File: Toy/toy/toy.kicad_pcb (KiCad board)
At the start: 2 copper layers, 190 x 120 mm, 25 parts, among them J1 Conn_01x07_Pin, J2 Conn_01x03_Pin, J3 Conn_01x03_Pin, J4 Conn_01x03_Pin

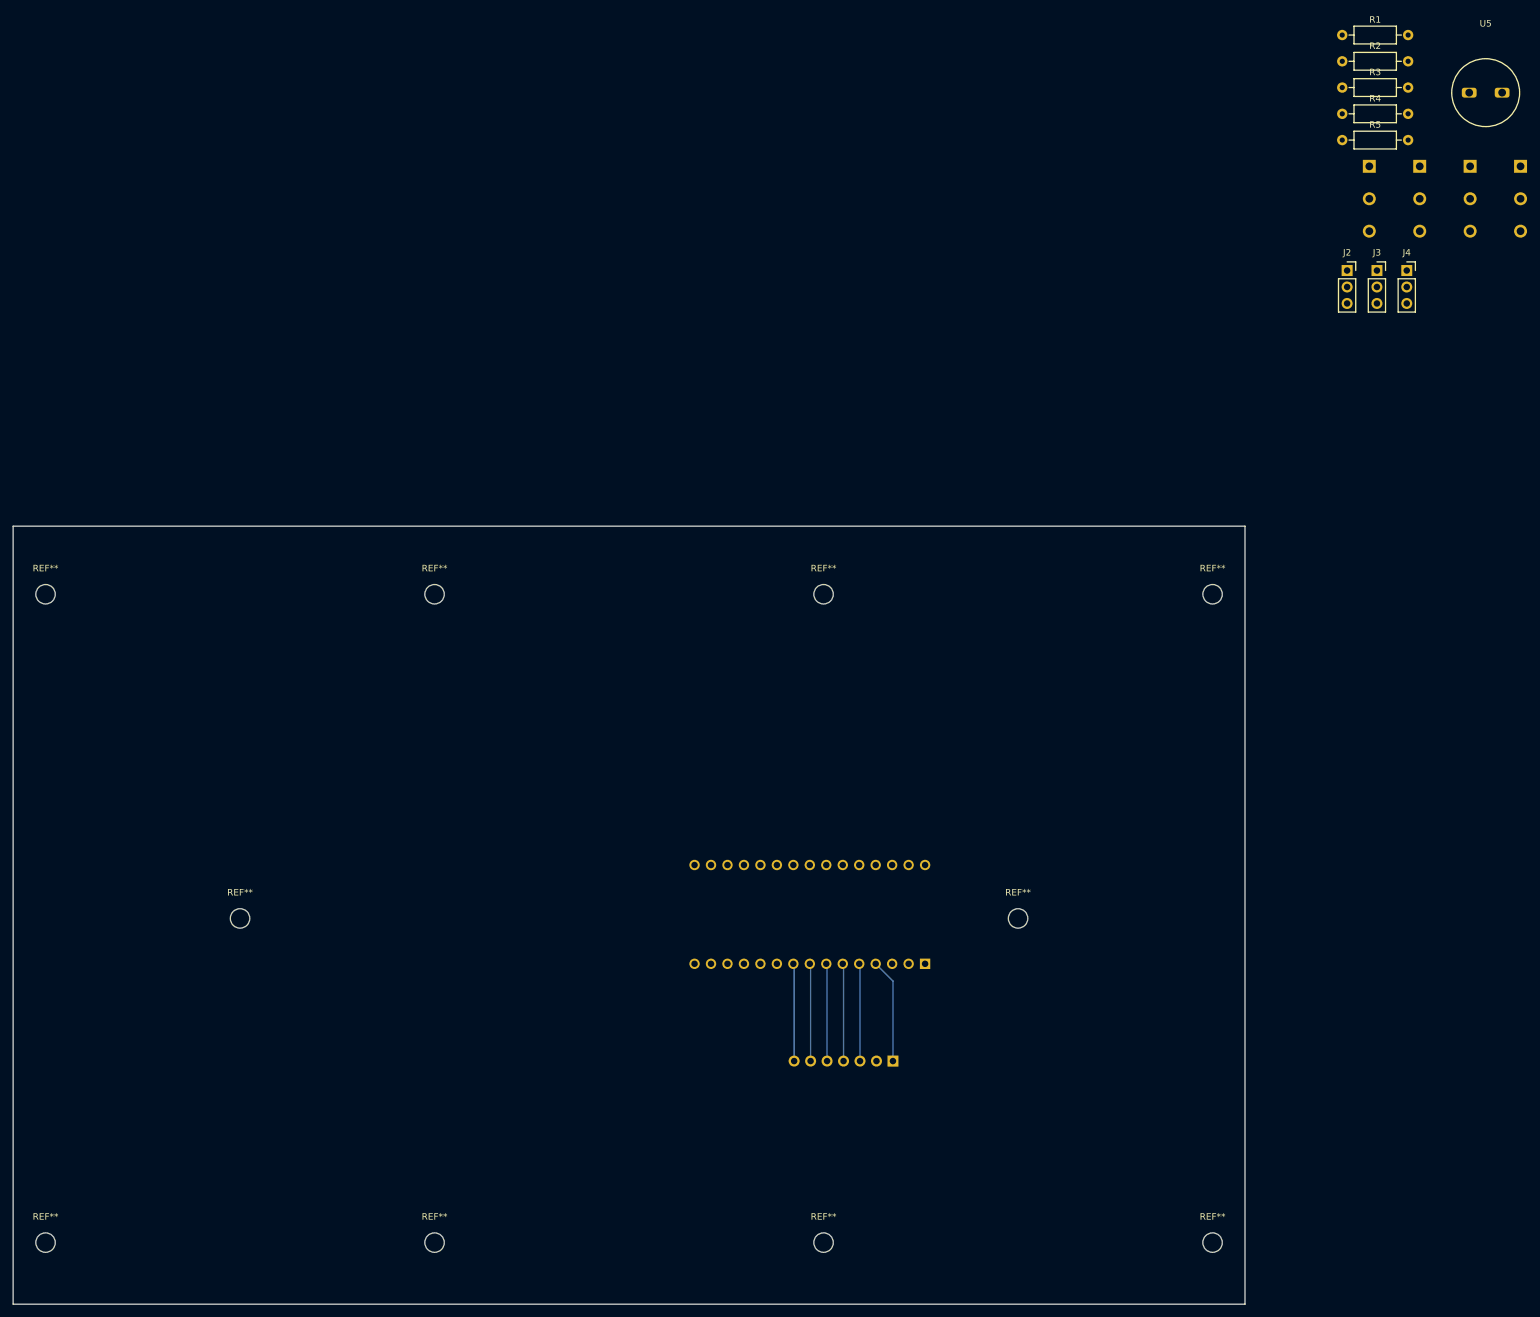
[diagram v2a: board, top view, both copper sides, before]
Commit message: V2.1
Ground fill added
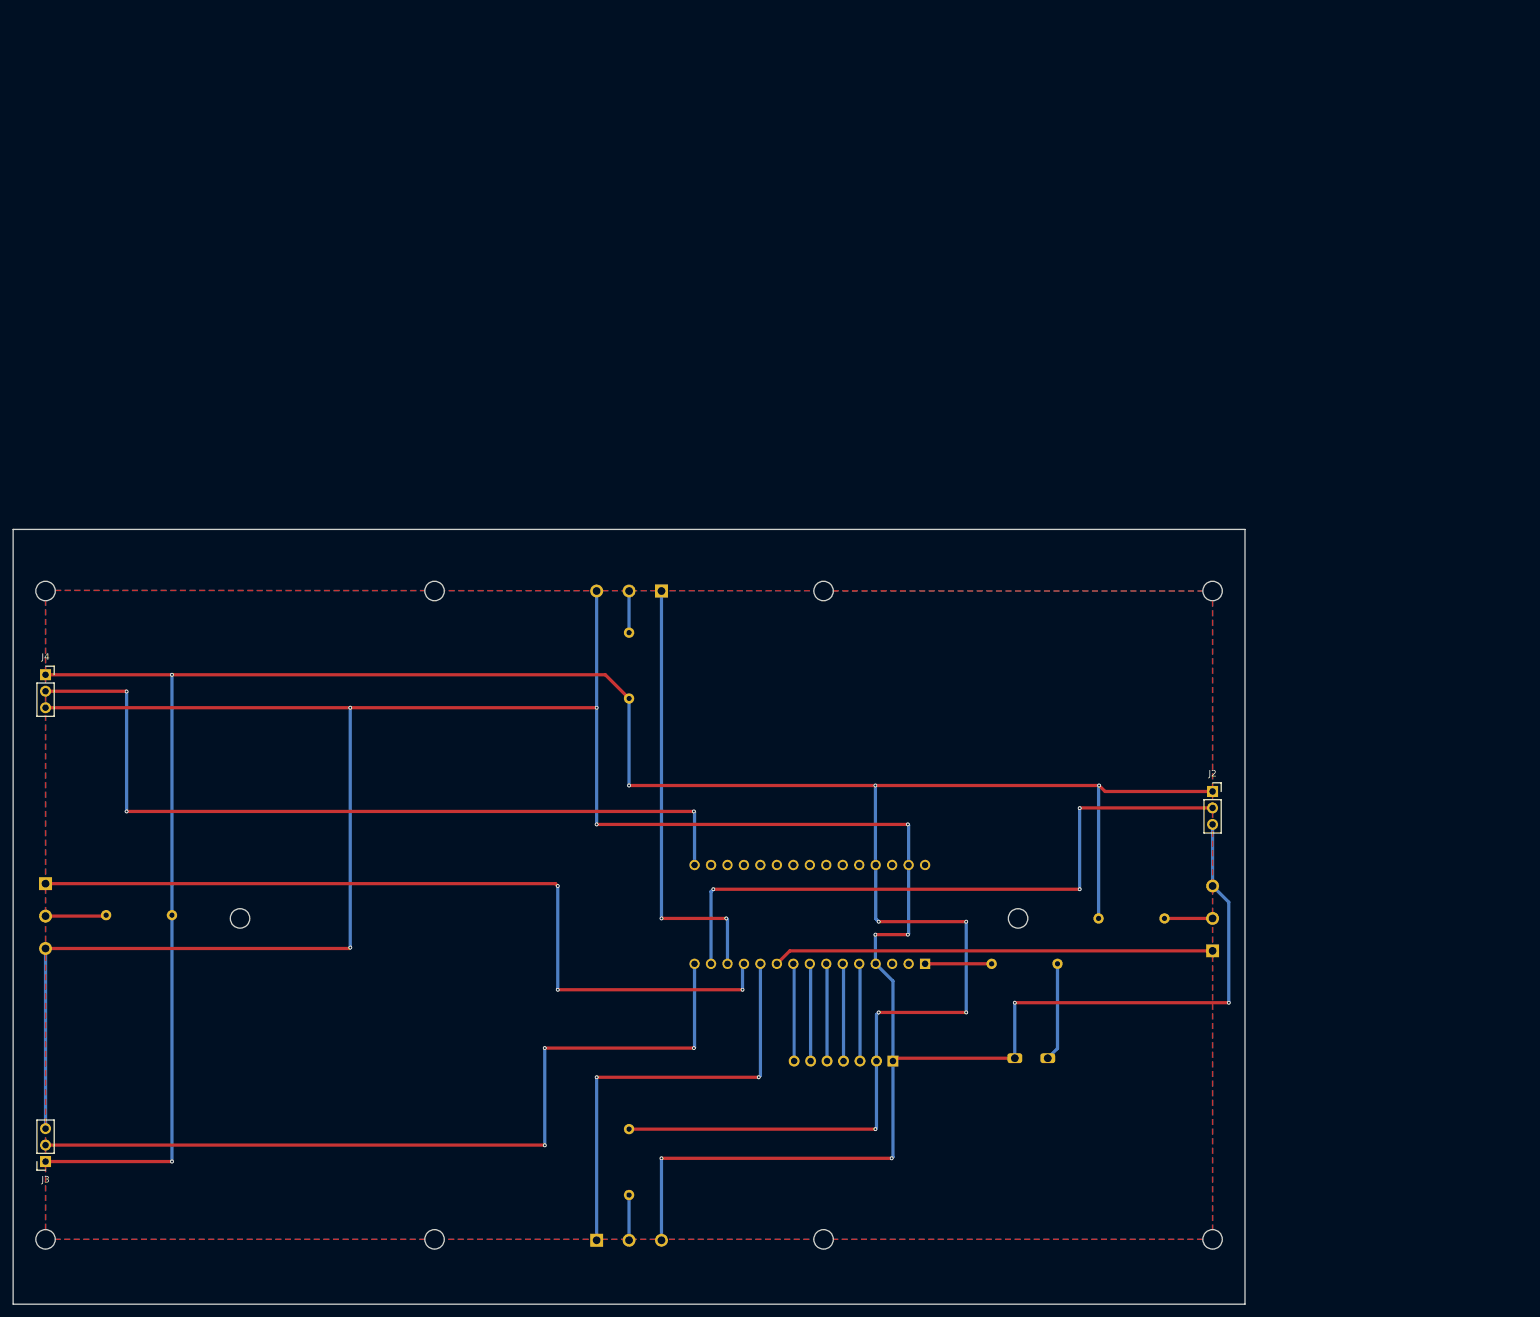
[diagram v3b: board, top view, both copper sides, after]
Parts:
- R1, R2, R3, R4, R5, U5: moved to B.Cu
- moved J3 247.1 mm to (46.5, 129.0), turned to 180 degrees
- moved U2 239.1 mm to (41.5, 99.1)
- moved R2 223.4 mm to (66.0, 91.0), turned to 180 degrees
- moved J4 219.0 mm to (46.5, 53.9)
- moved U3 196.1 mm to (144.5, 146.1), turned to 90 degrees
- moved R3 194.7 mm to (136.5, 124.0), turned to -90 degrees
- moved U5 164.6 mm to (198.5, 102.9), turned to 180 degrees
- moved U4 148.3 mm to (128.5, 36.0), turned to -90 degrees
- moved R4 142.2 mm to (136.5, 57.6), turned to 90 degrees
- moved R1 141.3 mm to (208.9, 91.5)
- moved R5 134.4 mm to (202.6, 98.5), turned to 180 degrees
- moved U1 96.1 mm to (231.5, 83.5), turned to 180 degrees
- moved J2 83.0 mm to (226.5, 71.9)
- moved REF** 0.50 mm to (106.5, 41.0)
- moved REF** 0.50 mm to (166.5, 141.0)
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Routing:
- net GND: track 16.1 -> 476.5 mm, vias 0 -> 11
- net VDD: track 0.00 -> 428.8 mm, vias 0 -> 10
- net /LED2_ctrl: track 0.00 -> 128.1 mm, vias 0 -> 3
- net /C_sw3: track 0.00 -> 127.9 mm, vias 0 -> 3
- net /LED3_ctrl: track 0.00 -> 126.8 mm, vias 0 -> 3
- net /LED1_ctrl: track 0.00 -> 101.2 mm, vias 0 -> 3
- net /C_sw2: track 0.00 -> 68.1 mm, vias 0 -> 2
- net /C_sw1: track 0.00 -> 68.0 mm
- net /C_sw4: track 0.00 -> 67.1 mm, vias 0 -> 2
- net Net-(U5-Vdd): track 0.00 -> 15.2 mm
- net /BUZZ: track 0.00 -> 10.3 mm
- net Net-(U2-NO): track 0.00 -> 9.53 mm
- net Net-(U1-NO): track 0.00 -> 7.42 mm
- net Net-(U3-NO): track 0.00 -> 7.34 mm
- net Net-(U4-NO): track 0.00 -> 5.92 mm
- added copper zone on B.Cu, net GND
- added copper zone on F.Cu, net GND
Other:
- board size 190 x 120 mm -> 190 x 119.5 mm
- board text added: "GND"

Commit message: Led directionality altered
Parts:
- moved J3 5.00 mm to (46.5, 124.0), turned to 0 degrees
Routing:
- net GND: track 476.5 -> 515.0 mm, vias 11 -> 10
- net VDD: track 428.8 -> 423.8 mm
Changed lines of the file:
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@@
 	(footprint "Connector_PinSocket_2.54mm:PinSocket_1x03_P2.54mm_Vertical"
 		(layer "F.Cu")
-		(at 46.5 129 180)
+		(at 46.5 124)
 		(descr "Through hole straight socket strip, 1x03, 2.54mm pitch, single row (from Kicad 4.0.7), script generated")
 		(tags "Through hole socket strip THT 1x03 2.54mm single row")
@@
 		)
 		(property "Footprint" "Connector_PinSocket_2.54mm:PinSocket_1x03_P2.54mm_Vertical"
-			(at 0 0 180)
+			(at 0 0 0)
 			(unlocked yes)
 			(layer "F.Fab")
@@
 		)
 		(property "Datasheet" ""
-			(at 0 0 180)
+			(at 0 0 0)
 			(unlocked yes)
 			(layer "F.Fab")
@@
 		)
 		(property "Description" "Generic connector, single row, 01x03, script generated"
-			(at 0 0 180)
+			(at 0 0 0)
 			(unlocked yes)
 			(layer "F.Fab")
@@
 		(attr through_hole)
 		(fp_line
-			(start 1.33 1.27)
-			(end 1.33 6.41)
+			(start -1.33 1.27)
+			(end -1.33 6.41)
 			(stroke
 				(width 0.12)
@@
 		)
 		(fp_line
-			(start 1.33 -1.33)
-			(end 1.33 0)
+			(start -1.33 1.27)
+			(end 1.33 1.27)
 			(stroke
 				(width 0.12)
@@
 		)
 		(fp_line
-			(start 0 -1.33)
-			(end 1.33 -1.33)
+			(start -1.33 6.41)
+			(end 1.33 6.41)
 			(stroke
 				(width 0.12)
@@
 		)
 		(fp_line
-			(start -1.33 6.41)
-			(end 1.33 6.41)
+			(start 0 -1.33)
+			(end 1.33 -1.33)
 			(stroke
 				(width 0.12)
@@
 		)
 		(fp_line
-			(start -1.33 1.27)
-			(end 1.33 1.27)
+			(start 1.33 -1.33)
+			(end 1.33 0)
 			(stroke
 				(width 0.12)
@@
 		)
 		(fp_line
-			(start -1.33 1.27)
-			(end -1.33 6.41)
+			(start 1.33 1.27)
+			(end 1.33 6.41)
 			(stroke
 				(width 0.12)
@@
 		)
 		(fp_line
-			(start 1.75 6.85)
-			(end -1.8 6.85)
+			(start -1.8 -1.8)
+			(end 1.75 -1.8)
 			(stroke
 				(width 0.05)
@@
 		)
 		(fp_line
-			(start 1.75 -1.8)
-			(end 1.75 6.85)
+			(start -1.8 6.85)
+			(end -1.8 -1.8)
 			(stroke
 				(width 0.05)
@@
 		)
 		(fp_line
-			(start -1.8 6.85)
-			(end -1.8 -1.8)
+			(start 1.75 -1.8)
+			(end 1.75 6.85)
 			(stroke
 				(width 0.05)
@@
 		)
 		(fp_line
-			(start -1.8 -1.8)
-			(end 1.75 -1.8)
+			(start 1.75 6.85)
+			(end -1.8 6.85)
 			(stroke
 				(width 0.05)
@@
 		)
 		(fp_line
-			(start 1.27 6.35)
-			(end -1.27 6.35)
+			(start -1.27 -1.27)
+			(end 0.635 -1.27)
 			(stroke
 				(width 0.1)
@@
 		)
 		(fp_line
-			(start 1.27 -0.635)
-			(end 1.27 6.35)
+			(start -1.27 6.35)
+			(end -1.27 -1.27)
 			(stroke
 				(width 0.1)
@@
 		)
 		(fp_line
-			(start -1.27 6.35)
-			(end -1.27 -1.27)
+			(start 1.27 -0.635)
+			(end 1.27 6.35)
 			(stroke
 				(width 0.1)
@@
 		)
 		(fp_line
-			(start -1.27 -1.27)
-			(end 0.635 -1.27)
+			(start 1.27 6.35)
+			(end -1.27 6.35)
 			(stroke
 				(width 0.1)
@@
 		)
 		(pad "1" thru_hole rect
-			(at 0 0 180)
+			(at 0 0)
 			(size 1.7 1.7)
 			(drill 1)
@@
 		)
 		(pad "2" thru_hole oval
-			(at 0 2.54 180)
+			(at 0 2.54)
 			(size 1.7 1.7)
 			(drill 1)
@@
 		)
 		(pad "3" thru_hole oval
-			(at 0 5.08 180)
+			(at 0 5.08)
 			(size 1.7 1.7)
 			(drill 1)
@@
 		)
 		(property "Value" "Arduino_Nano_Every"
-			(at 8.89 -19.05 360)
+			(at 8.89 -19.05 0)
 			(layer "B.Fab")
 			(effects
@@
 		)
 		(fp_text user "${REFERENCE}"
-			(at 6.35 -19.05 360)
+			(at 6.35 -19.05 0)
 			(layer "B.Fab")
 			(effects
@@
 		)
 		(fp_text user "${REFERENCE}"
-			(at 0 -7.62 360)
+			(at 0 -7.62 0)
 			(layer "B.Fab")
 			(effects
@@
 	)
 	(segment
+		(start 93.3625 96.1375)
+		(end 46.3625 96.1375)
+		(width 0.5)
+		(layer "F.Cu")
+		(net 9)
+	)
+	(segment
 		(start 141.5 128.5)
 		(end 177 128.5)
@@
 	)
 	(segment
-		(start 46.3625 96.1375)
-		(end 93.3625 96.1375)
+		(start 226.5 77)
+		(end 179.5 77)
 		(width 0.5)
 		(layer "F.Cu")
@@
 	)
 	(segment
-		(start 93.3625 96.1375)
-		(end 93.5 96)
+		(start 93 129)
+		(end 92.92 129.08)
 		(width 0.5)
 		(layer "F.Cu")
@@
 	)
 	(segment
-		(start 196 104.5)
-		(end 229 104.5)
+		(start 177.638172 113.061828)
+		(end 177.2 113.5)
 		(width 0.5)
 		(layer "F.Cu")
@@
 	)
 	(segment
-		(start 177.638172 113.061828)
-		(end 177.2 113.5)
+		(start 92.92 129.08)
+		(end 46.5 129.08)
+		(width 0.5)
+		(layer "F.Cu")
+		(net 9)
+	)
+	(segment
+		(start 93.5 96)
+		(end 93.3625 96.1375)
 		(width 0.5)
 		(layer "F.Cu")
@@
 	)
 	(via
-		(at 131.5 77)
+		(at 93 129)
 		(size 0.6)
 		(drill 0.3)
@@
 	)
 	(via
-		(at 177 128.5)
+		(at 131.5 77)
 		(size 0.6)
 		(drill 0.3)
@@
 	)
 	(via
-		(at 196 104.5)
+		(at 177 128.5)
 		(size 0.6)
 		(drill 0.3)
@@
 		(net 9)
 	)
-	(via
-		(at 229 104.5)
-		(size 0.6)
-		(drill 0.3)
-		(layers "F.Cu" "B.Cu")
-		(net 9)
-	)
-	(segment
-		(start 93.5 96)
-		(end 93.5 59)
-		(width 0.5)
-		(layer "B.Cu")
-		(net 9)
-	)
 	(segment
 		(start 177.2 128.3)
@@
 	)
 	(segment
-		(start 196 113.061828)
-		(end 196 104.5)
+		(start 93.5 96)
+		(end 93.5 59)
 		(width 0.5)
 		(layer "B.Cu")
@@
 	)
 	(segment
-		(start 226.5 77)
-		(end 226.5 86.5)
+		(start 93.5 128.5)
+		(end 93 129)
 		(width 0.5)
 		(layer "B.Cu")
@@
 	)
 	(segment
-		(start 46.5 96.275)
-		(end 46.3625 96.1375)
+		(start 226.5 77)
+		(end 226.5 86.5)
 		(width 0.5)
 		(layer "B.Cu")
@@
 	)
 	(segment
-		(start 229 89)
-		(end 226.5 86.5)
+		(start 46.5 96.275)
+		(end 46.3625 96.1375)
 		(width 0.5)
 		(layer "B.Cu")
@@
 	)
 	(segment
-		(start 229 104.5)
-		(end 229 89)
-		(width 0.5)
-		(layer "B.Cu")
-		(net 9)
-	)
-	(segment
-		(start 46.5 123.92)
-		(end 46.5 96.275)
+		(start 179.62 83.26)
+		(end 179.62 93.88)
 		(width 0.5)
 		(layer "B.Cu")
@@
 	)
 	(segment
-		(start 179.62 83.26)
-		(end 179.62 93.88)
+		(start 93.5 96)
+		(end 93.5 128.5)
 		(width 0.5)
 		(layer "B.Cu")
@@
 	)
 	(segment
-		(start 46.5 129)
-		(end 66 129)
+		(start 209 71)
+		(end 174.5 71)
 		(width 0.5)
 		(layer "F.Cu")
@@
 	)
 	(segment
-		(start 209 71)
-		(end 174.5 71)
+		(start 46.5 124)
+		(end 66 124)
 		(width 0.5)
 		(layer "F.Cu")
@@
 	)
 	(via
-		(at 66 53.92)
+		(at 66 124)
 		(size 0.6)
 		(drill 0.3)
@@
 	)
 	(via
-		(at 66 129)
+		(at 66 53.92)
 		(size 0.6)
 		(drill 0.3)
@@
 	)
 	(segment
-		(start 66 129)
-		(end 66 91)
-		(width 0.5)
-		(layer "B.Cu")
-		(net 22)
-	)
-	(segment
 		(start 174.66 113.5)
 		(end 174.66 106.34)
@@
 		(width 0.5)
 		(layer "B.Cu")
+		(net 22)
+	)
+	(segment
+		(start 66 124)
+		(end 66 91)
+		(width 0.5)
+		(layer "B.Cu")

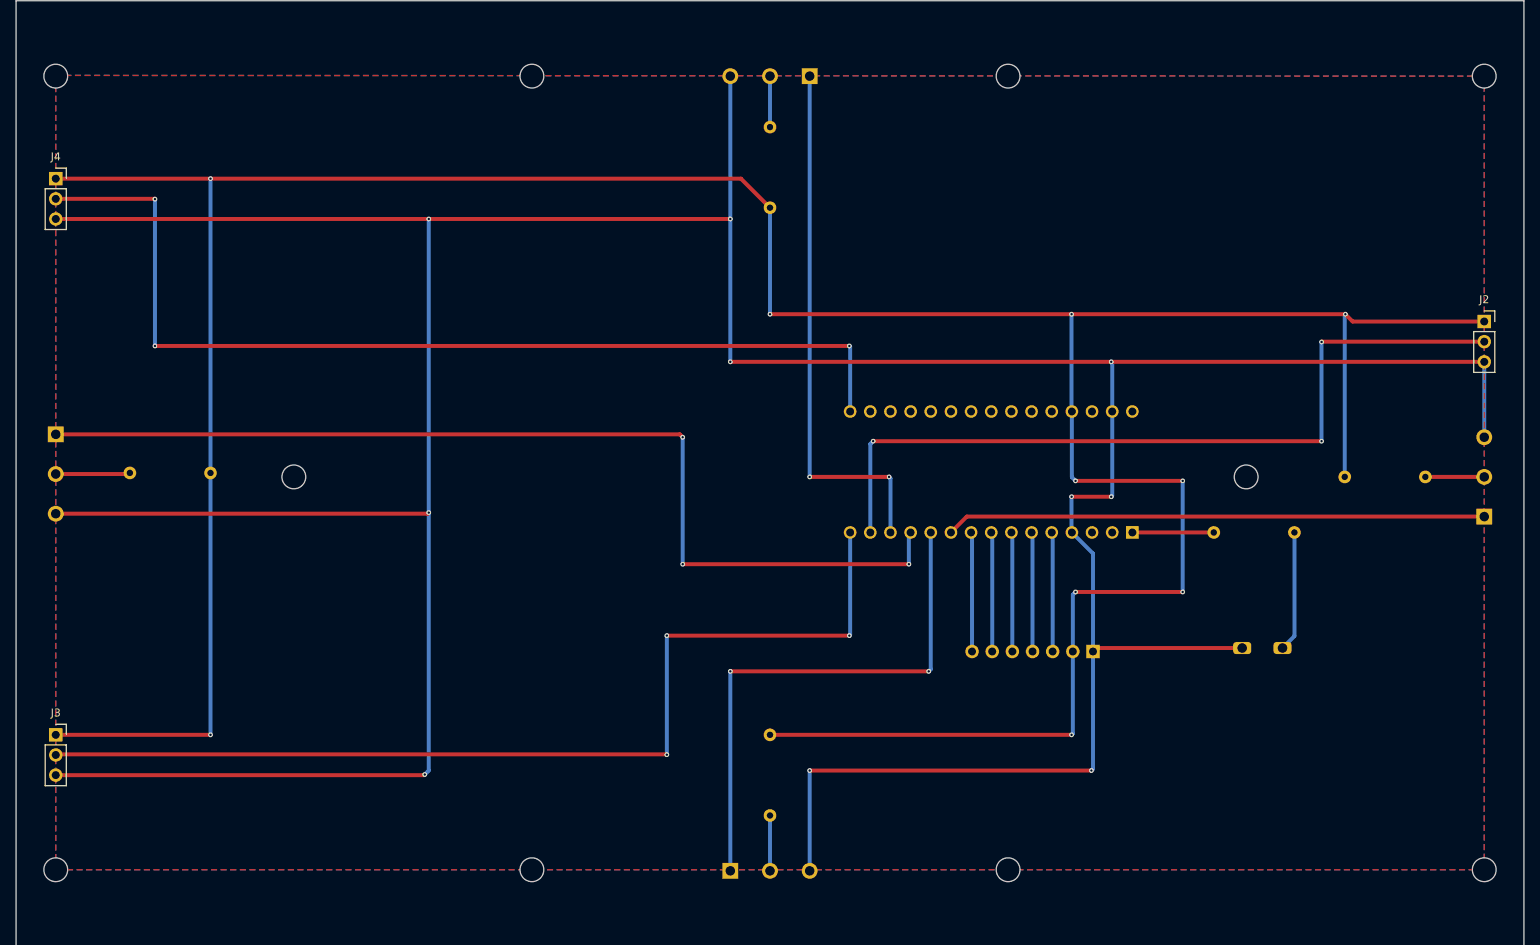
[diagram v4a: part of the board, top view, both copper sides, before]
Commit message: V3.0
Led orientation fixed, bigger ground fill
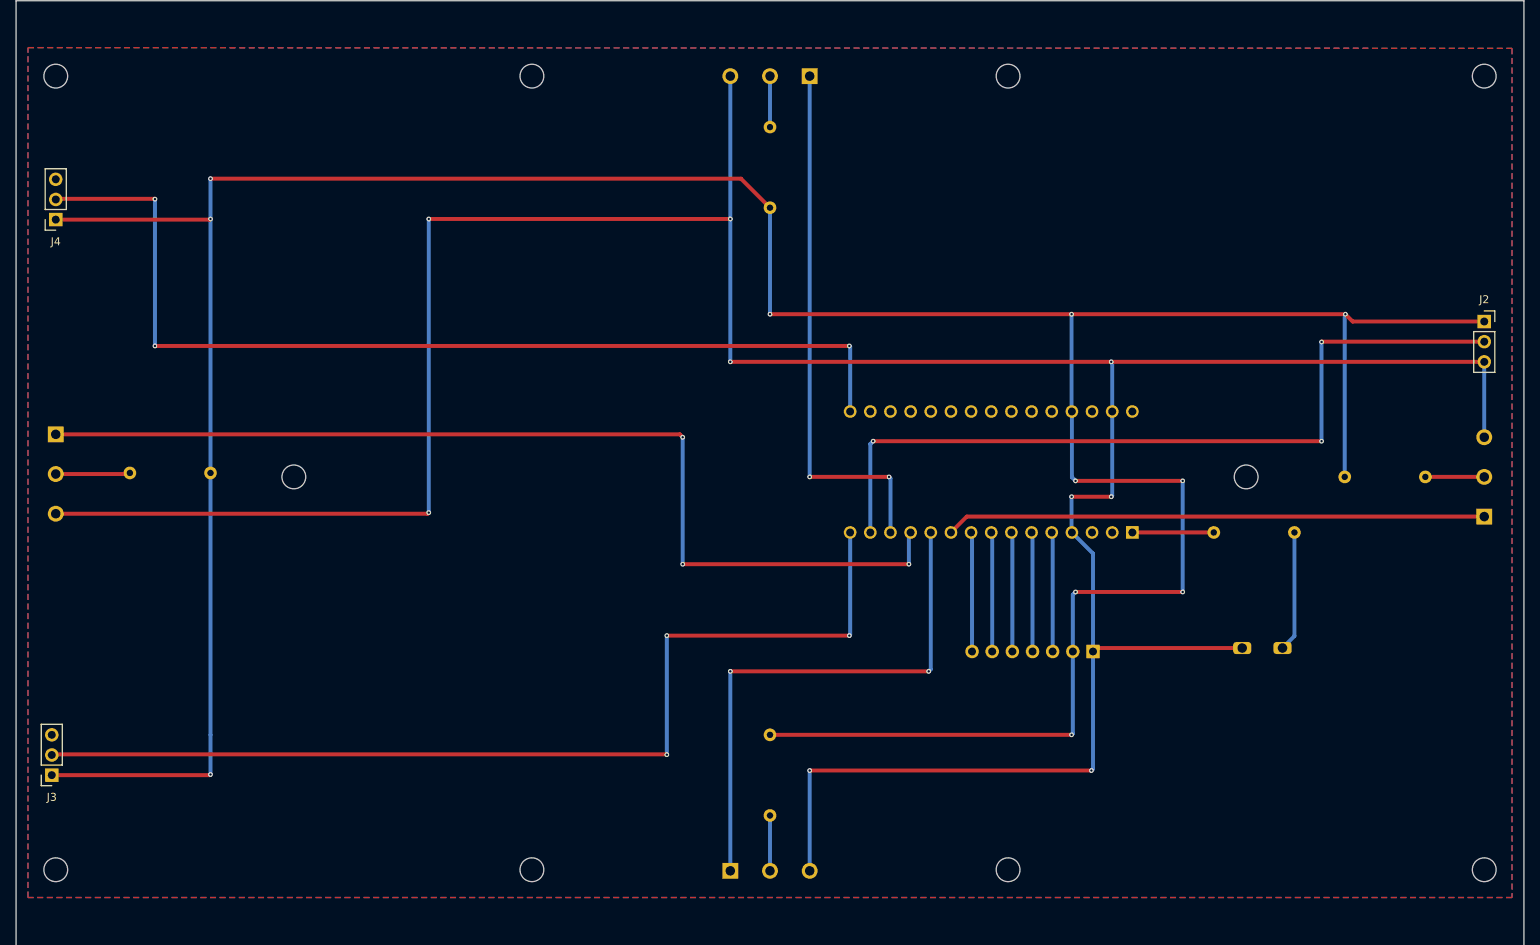
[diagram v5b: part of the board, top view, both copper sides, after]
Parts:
- moved J4 5.16 mm to (46.5, 59.1), turned to 180 degrees
- moved J3 5.10 mm to (46.0, 129.1), turned to 180 degrees
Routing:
- net GND: track 515.0 -> 388.3 mm, vias 10 -> 9
- net VDD: track 423.8 -> 429.4 mm, vias 10 -> 11
